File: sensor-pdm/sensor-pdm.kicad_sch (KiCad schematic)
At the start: 27 parts, among them J1 43045-0600, J2 43045-0800, J3 43045-1200

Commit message: pcb basically done, needs a bit of silkscreen
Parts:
- removed C1: 470u, Capacitor_THT:CP_Radial_D10.0mm_P5.00mm, symbol Device:C_Polarized
- removed D4, D5, D6, D7: Green, LED_SMD:LED_0603_1608Metric, symbol Device:LED
- removed H3: MountingHole_Pad, MountingHole:MountingHole_3.2mm_M3_Pad_Via, symbol Mechanical:MountingHole_Pad
- removed J1: 43045-0600, Connector_Molex:Molex_Micro-Fit_3.0_43045-0600_2x03_P3.00mm_Horizontal, symbol Connector_Generic:Conn_01x06
- removed J2: 43045-0800, Connector_Molex:Molex_Micro-Fit_3.0_43045-0800_2x04_P3.00mm_Horizontal, symbol Connector_Generic:Conn_01x08
- removed L1: 6.8u, SamacSys:SPM6530, symbol Device:L
- removed R26: 1k, Resistor_SMD:R_0603_1608Metric, symbol Device:R
- added C1, C2, C3, C4: 0.1uF, Capacitor_SMD:C_0603_1608Metric_Pad1.08x0.95mm_HandSolder, symbol Device:C
- added C5, C6: 1uF, Capacitor_SMD:C_0603_1608Metric_Pad1.08x0.95mm_HandSolder, symbol Device:C
- added D10, D11, D4, D5, D6, D7, D8, D9: D_TVS, SUFST:D_SOD-323_wide, symbol Device:D_TVS
- added FB1: FerriteBead, Inductor_SMD:L_0805_2012Metric_Pad1.05x1.20mm_HandSolder, symbol Device:FerriteBead
- added J1, J2: Conn_01x04, Connector_Molex:Molex_Micro-Fit_3.0_43045-0400_2x02_P3.00mm_Horizontal, symbol Connector_Generic:Conn_01x04
- added J4: Conn_01x12, Molex_Micro-Fit_3.0_43045-1200_2x06_P3.00mm_Horizontal, symbol Connector_Generic:Conn_01x12
- added R10, R11, R12, R13, R9: 10k, Resistor_SMD:R_0603_1608Metric_Pad0.98x0.95mm_HandSolder, symbol Device:R
- added R14, R15: 1k, Resistor_SMD:R_0603_1608Metric_Pad0.98x0.95mm_HandSolder, symbol Device:R
- added U1, U2: TPS25961, SUFST:TPS73733DRVR, symbol SUFST:TPS25961
- added U3: TVS1800DRV, Package_SON:WSON-6-1EP_2x2mm_P0.65mm_EP1x1.6mm, symbol Power_Protection:TVS1800DRV
- added U4: TVL767, Package_SO:HVSSOP-8-1EP_3x3mm_P0.65mm_EP1.57x1.89mm, symbol SUFST:TLV767
- D1: value Red -> Green; footprint LED_SMD:LED_0603_1608Metric -> LED_SMD:LED_0603_1608Metric_Pad1.05x0.95mm_HandSolder; Mouser Part Number 755-SML-D12U1WT86 -> 755-SML-D12P8WT86
- D2, D3: footprint LED_SMD:LED_0603_1608Metric -> LED_SMD:LED_0603_1608Metric_Pad1.05x0.95mm_HandSolder
- F1: value 5A -> 700mA; footprint Fuse:Fuse_0603_1608Metric -> Fuse:Fuse_0603_1608Metric_Pad1.05x0.95mm_HandSolder
- J3: value 43045-1200 -> Conn_01x12; footprint Connector_Molex:Molex_Micro-Fit_3.0_43045-1200_2x06_P3.00mm_Horizontal -> Molex_Micro-Fit_3.0_43045-1200_2x06_P3.00mm_Horizontal; To Order INV -> (none)
- R1, R2, R3, R4, R5, R6, R7: footprint Resistor_SMD:R_0603_1608Metric -> Resistor_SMD:R_0603_1608Metric_Pad0.98x0.95mm_HandSolder
- R8: value 1k -> 10k; footprint Resistor_SMD:R_0603_1608Metric -> Resistor_SMD:R_0603_1608Metric_Pad0.98x0.95mm_HandSolder
- renumbered H4 to H2, H2 to H3, H5 to H4
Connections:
- net +GLV_fused is gone; now on an unnamed net: F1.1
- net APPS2.GND is gone; now on net GND: J3.1 (Pin_1)
- net Analogue Power/Vout is gone; now on net GND: J3.12 (Pin_12)
- net Analogue Power1/Vout is gone; now on net +PERF_OUT: J3.11 (Pin_11)
- net Analogue Power2/Vout is gone; now on net GND: J3.10 (Pin_10)
- net Analogue Power3/Vout is gone; now on net GND: J3.9 (Pin_9)
- net +GLV: now also J1.1 (Pin_1), J1.2 (Pin_2), U3.4 (IN), U3.5 (IN), U3.6 (IN)
- net GND: now also J3.7 (Pin_7), R3.2, R6.2, R7.1, R8.1, C1.1, C2.1, C3.1, C4.1, C5.1, C6.1, D10.1 (A1), D11.1 (A1), D4.1 (A1), D5.1 (A1), D6.1 (A1), D7.1 (A1), D8.1 (A1), D9.1 (A1), J1.3 (Pin_3), J1.4 (Pin_4), J2.2 (Pin_2), J4.10 (Pin_10), J4.12 (Pin_12), J4.3 (Pin_3), J4.4 (Pin_4), J4.6 (Pin_6), J4.7 (Pin_7), J4.9 (Pin_9), R10.1, R11.1, R13.2, R15.2, R9.1, U1.4 (GND), U1.7 (EXP), U2.4 (GND), U2.7 (EXP), U3.1 (GND), U3.2 (GND), U3.3 (GND), U3.7 (GND), U4.4 (GND), U4.6 (GND), U4.9 (EXP); no longer J3.2 (Pin_2), J3.5 (Pin_5)
- net at D3.2 (A): now also FB1.1; no longer R3.2
- net at R7.2: now also U1.3 (ILIM)
- net +LDO_8V: now reaches R1.1
- net +LDO_8V: now also R4.1, C1.2, C2.2, C6.2, J2.1 (Pin_1), R12.1, U1.6 (IN), U2.6 (IN), U4.1 (OUT); no longer D1.2 (A)
- net at R4.2: now also R5.1, U2.5 (EN/UVLO)
- net at R2.1: now also R1.2, U1.5 (EN/UVLO); no longer D2.2 (A)
- net at R5.2: now also R6.1, U2.2 (OVLO)
- removed net +12V: R1.2, R2.2, R3.1, R4.1, R5.1, R6.1, R7.1
- net APPS1.PWR renamed +PERF_OUT
- net +PERF_OUT: now also D2.2 (A), J3.2 (Pin_2), J3.5 (Pin_5), C4.2, D10.2 (A2), D11.2 (A2), D4.2 (A2), D6.2 (A2), D8.2 (A2), D9.2 (A2), J2.3 (Pin_3), J4.11 (Pin_11), J4.5 (Pin_5), U2.1 (OUT); no longer R8.1
- net APPS2.PWR: no longer names the net of R8.2
- net APPS2.PWR: now also U2.3 (ILIM); no longer J3.7 (Pin_7)
- net Analogue Power/PG: no longer names the net of D3.1 (K)
- net Analogue Power/PG: now also R11.2
- net Power/PG: no longer names the net of D2.1 (K)
- net Power/PG: now also R10.2
- net Power/~{CC}: no longer names the net of D1.1 (K)
- net Power/~{CC}: now also R9.2
- new net: J4.1 (Pin_1), R15.1
- new net: R12.2, R13.1, U4.2 (FB)
- new net: R2.2, R3.1, U1.2 (OVLO)
- new net: J4.2 (Pin_2), R14.2
- new net: C5.2, FB1.2, U4.5 (EN), U4.8 (IN)
- new net +SCS_OUT: C3.2, D1.2 (A), D5.2 (A2), D7.2 (A2), J2.4 (Pin_4), J4.8 (Pin_8), R14.1, U1.1 (OUT)
- no-connect marks 0 -> 2
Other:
- removed sheet Analogue Power
- removed sheet Analogue Power1
- removed sheet Analogue Power2
- removed sheet Analogue Power3
- removed sheet Analogue Power4
- removed sheet Power
- note added: "Plug these into spare VCU inputs so u know when they switch off"
- note removed: "1, 2, 4, 5, VCU Power"
- moved on the sheet: H1, H2, H3, H4

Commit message: Updated silk and tweaked fills
Ready for v1.1 release
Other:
- company: (none) -> Southampton University Formula Student Team
- title: (none) -> Stag 12 Sensor PDM
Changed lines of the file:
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@@
 	(generator_version "9.0")
 	(paper "A3")
+	(title_block
+		(title "Stag 12 Sensor PDM")
+		(date "2026-05-04")
+		(rev "1.1.0")
+		(company "Southampton University Formula Student Team")
+		(comment 1 "Stag 12")
+		(comment 2 "Annabel Owen")
+		(comment 3 "Adam Eastman, Ray Wang")
+	)
 	(text "Plug these into spare VCU inputs so u know when they switch off"
 		(exclude_from_sim no)

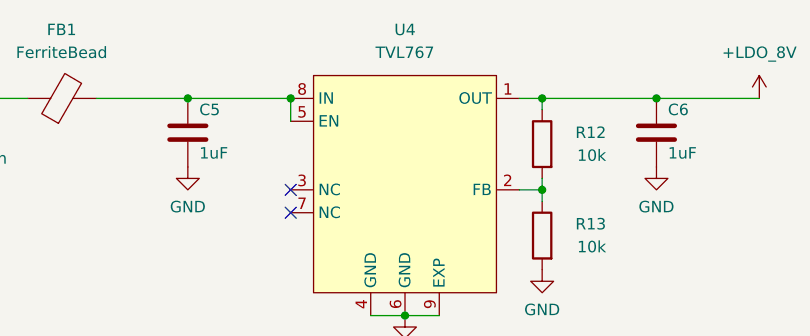
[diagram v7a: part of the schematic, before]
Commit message: change silkscreen, sent off to aisler
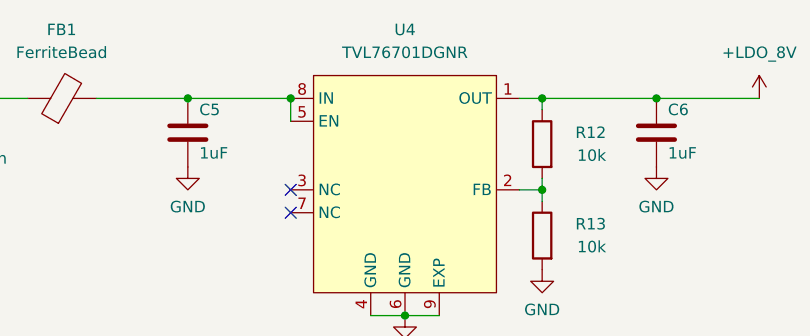
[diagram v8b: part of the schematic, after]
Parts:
- U4: value TVL767 -> TVL76701DGNR
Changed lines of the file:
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@@
 			)
 		)
-		(property "Value" "TVL767"
+		(property "Value" "TVL76701DGNR"
 			(at 176.53 36.83 0)
 			(effects
